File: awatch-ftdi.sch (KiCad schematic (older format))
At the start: 44 parts, among them J801 Molex 1050170001, J802 Conn_01x06, U801 AT93C46DN-SH-T, U802 MCP1703A-3302_SOT223, U803 FT2232HL, Y801 FH1200004

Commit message: approx. final layout
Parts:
- C801, C802, C803, C809, C810, C811, C812, C813, C814, C815, C816, C817, C818: value .1µF -> 0.1µF X7R; DigiKey PN (none) -> 1276-1061-1-ND
- C804, C806: value 4.7µF -> 4.7µF X7R; DigiKey PN (none) -> 1276-2087-1-ND
- C805, C807: value 22pF -> 22pF NP0; DigiKey PN (none) -> 399-7874-1-ND
- C808: value 3.3µF -> 4.7µF X7R; DigiKey PN (none) -> 1276-2087-1-ND
- J801: DigiKey PN (none) -> WM1399CT-ND
- U801: DigiKey PN (none) -> AT93C46DN-SH-TCT-ND AT93C46DN-SH-TCT-ND
- U802: DigiKey PN (none) -> MCP1703AT-3302E/DBCT-ND
- U803: DigiKey PN (none) -> 768-1024-1-ND
- Y801: DigiKey PN (none) -> FH1200004CT-ND
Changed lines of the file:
@@
 $Descr A4 11693 8268
 encoding utf-8
-Sheet 8 9
+Sheet 8 10
 Title "AWatch2"
 Date ""
@@
 F 2 "Package_QFP:LQFP-64_10x10mm_P0.5mm" H 5750 4450 50  0001 C CNN
 F 3 "http://www.ftdichip.com/Products/ICs/FT2232H.html" H 5750 4450 50  0001 C CNN
+F 4 "768-1024-1-ND" H 0   0   50  0001 C CNN "DigiKey PN"
 	1    5750 4450
 	1    0    0    -1
@@
 F 2 "Package_TO_SOT_SMD:SOT-223-3_TabPin2" H 3650 2750 50  0001 C CNN
 F 3 "http://ww1.microchip.com/downloads/en/DeviceDoc/20005122B.pdf" H 3650 2500 50  0001 C CNN
+F 4 "MCP1703AT-3302E/DBCT-ND" H 0   0   50  0001 C CNN "DigiKey PN"
 	1    3650 2550
 	1    0    0    -1
@@
 F 2 "Package_SO:SOIC-8_3.9x4.9mm_P1.27mm" H 2150 5350 50  0001 C CNN
 F 3 "http://ww1.microchip.com/downloads/en/DeviceDoc/20001749K.pdf" H 2150 5350 50  0001 C CNN
+F 4 "AT93C46DN-SH-TCT-NDAT93C46DN-SH-TCT-ND" H 0   0   50  0001 C CNN "DigiKey PN"
 	1    2150 5350
 	1    0    0    -1
@@
 P 1250 5300
 F 0 "C801" H 1342 5346 50  0000 L CNN
-F 1 ".1µF" H 1342 5255 50  0000 L CNN
+F 1 "0.1µF X7R" H 1342 5255 50  0000 L CNN
 F 2 "Capacitor_SMD:C_0603_1608Metric" H 1250 5300 50  0001 C CNN
 F 3 "~" H 1250 5300 50  0001 C CNN
+F 4 "1276-1061-1-ND" H 0   0   50  0001 C CNN "DigiKey PN"
 	1    1250 5300
 	1    0    0    -1
@@
 P 4050 2700
 F 0 "C803" H 4142 2746 50  0000 L CNN
-F 1 ".1µF" H 4142 2655 50  0000 L CNN
+F 1 "0.1µF X7R" H 4142 2655 50  0000 L CNN
 F 2 "Capacitor_SMD:C_0603_1608Metric" H 4050 2700 50  0001 C CNN
 F 3 "~" H 4050 2700 50  0001 C CNN
+F 4 "1276-1061-1-ND" H 0   0   50  0001 C CNN "DigiKey PN"
 	1    4050 2700
 	1    0    0    -1
@@
 P 3150 2700
 F 0 "C802" H 3242 2746 50  0000 L CNN
-F 1 ".1µF" H 3242 2655 50  0000 L CNN
+F 1 "0.1µF X7R" H 3242 2655 50  0000 L CNN
 F 2 "Capacitor_SMD:C_0603_1608Metric" H 3150 2700 50  0001 C CNN
 F 3 "~" H 3150 2700 50  0001 C CNN
+F 4 "1276-1061-1-ND" H 0   0   50  0001 C CNN "DigiKey PN"
 	1    3150 2700
 	1    0    0    -1
@@
 P 4450 2950
 F 0 "C808" H 4358 2996 50  0000 R CNN
-F 1 "3.3µF" H 4358 2905 50  0000 R CNN
+F 1 "4.7µF X7R" H 4358 2905 50  0000 R CNN
 F 2 "Capacitor_SMD:C_0603_1608Metric" H 4450 2950 50  0001 C CNN
 F 3 "~" H 4450 2950 50  0001 C CNN
+F 4 "1276-2087-1-ND" H 0   0   50  0001 C CNN "DigiKey PN"
 	1    4450 2950
 	1    0    0    -1
@@
 P 4550 1500
 F 0 "C809" H 4642 1546 50  0000 L CNN
-F 1 ".1µF" H 4642 1455 50  0000 L CNN
+F 1 "0.1µF X7R" H 4642 1455 50  0000 L CNN
 F 2 "Capacitor_SMD:C_0603_1608Metric" H 4550 1500 50  0001 C CNN
 F 3 "~" H 4550 1500 50  0001 C CNN
+F 4 "1276-1061-1-ND" H 0   0   50  0001 C CNN "DigiKey PN"
 	1    4550 1500
 	1    0    0    -1
@@
 P 4750 1500
 F 0 "C810" H 4842 1546 50  0000 L CNN
-F 1 ".1µF" H 4842 1455 50  0000 L CNN
+F 1 "0.1µF X7R" H 4842 1455 50  0000 L CNN
 F 2 "Capacitor_SMD:C_0603_1608Metric" H 4750 1500 50  0001 C CNN
 F 3 "~" H 4750 1500 50  0001 C CNN
+F 4 "1276-1061-1-ND" H 0   0   50  0001 C CNN "DigiKey PN"
 	1    4750 1500
 	1    0    0    -1
@@
 P 6000 1150
 F 0 "C811" H 6092 1196 50  0000 L CNN
-F 1 ".1µF" H 6092 1105 50  0000 L CNN
+F 1 "0.1µF X7R" H 6092 1105 50  0000 L CNN
 F 2 "Capacitor_SMD:C_0603_1608Metric" H 6000 1150 50  0001 C CNN
 F 3 "~" H 6000 1150 50  0001 C CNN
+F 4 "1276-1061-1-ND" H 0   0   50  0001 C CNN "DigiKey PN"
 	1    6000 1150
 	1    0    0    -1
@@
 P 6350 1150
 F 0 "C812" H 6442 1196 50  0000 L CNN
-F 1 ".1µF" H 6442 1105 50  0000 L CNN
+F 1 "0.1µF X7R" H 6442 1105 50  0000 L CNN
 F 2 "Capacitor_SMD:C_0603_1608Metric" H 6350 1150 50  0001 C CNN
 F 3 "~" H 6350 1150 50  0001 C CNN
+F 4 "1276-1061-1-ND" H 0   0   50  0001 C CNN "DigiKey PN"
 	1    6350 1150
 	1    0    0    -1
@@
 P 6700 1150
 F 0 "C813" H 6792 1196 50  0000 L CNN
-F 1 ".1µF" H 6792 1105 50  0000 L CNN
+F 1 "0.1µF X7R" H 6792 1105 50  0000 L CNN
 F 2 "Capacitor_SMD:C_0603_1608Metric" H 6700 1150 50  0001 C CNN
 F 3 "~" H 6700 1150 50  0001 C CNN
+F 4 "1276-1061-1-ND" H 0   0   50  0001 C CNN "DigiKey PN"
 	1    6700 1150
 	1    0    0    -1
@@
 P 7050 1150
 F 0 "C814" H 7142 1196 50  0000 L CNN
-F 1 ".1µF" H 7142 1105 50  0000 L CNN
+F 1 "0.1µF X7R" H 7142 1105 50  0000 L CNN
 F 2 "Capacitor_SMD:C_0603_1608Metric" H 7050 1150 50  0001 C CNN
 F 3 "~" H 7050 1150 50  0001 C CNN
+F 4 "1276-1061-1-ND" H 0   0   50  0001 C CNN "DigiKey PN"
 	1    7050 1150
 	1    0    0    -1
@@
 P 7400 1150
 F 0 "C815" H 7492 1196 50  0000 L CNN
-F 1 ".1µF" H 7492 1105 50  0000 L CNN
+F 1 "0.1µF X7R" H 7492 1105 50  0000 L CNN
 F 2 "Capacitor_SMD:C_0603_1608Metric" H 7400 1150 50  0001 C CNN
 F 3 "~" H 7400 1150 50  0001 C CNN
+F 4 "1276-1061-1-ND" H 0   0   50  0001 C CNN "DigiKey PN"
 	1    7400 1150
 	1    0    0    -1
@@
 P 7750 1150
 F 0 "C816" H 7842 1196 50  0000 L CNN
-F 1 ".1µF" H 7842 1105 50  0000 L CNN
+F 1 "0.1µF X7R" H 7842 1105 50  0000 L CNN
 F 2 "Capacitor_SMD:C_0603_1608Metric" H 7750 1150 50  0001 C CNN
 F 3 "~" H 7750 1150 50  0001 C CNN
+F 4 "1276-1061-1-ND" H 0   0   50  0001 C CNN "DigiKey PN"
 	1    7750 1150
 	1    0    0    -1
@@
 P 8100 1150
 F 0 "C817" H 8192 1196 50  0000 L CNN
-F 1 ".1µF" H 8192 1105 50  0000 L CNN
+F 1 "0.1µF X7R" H 8192 1105 50  0000 L CNN
 F 2 "Capacitor_SMD:C_0603_1608Metric" H 8100 1150 50  0001 C CNN
 F 3 "~" H 8100 1150 50  0001 C CNN
+F 4 "1276-1061-1-ND" H 0   0   50  0001 C CNN "DigiKey PN"
 	1    8100 1150
 	1    0    0    -1
@@
 F 2 "Crystal:Crystal_SMD_2520-4Pin_2.5x2.0mm" H 3600 5850 50  0001 C CNN
 F 3 "~" H 3600 5850 50  0001 C CNN
+F 4 "FH1200004CT-ND" H 0   0   50  0001 C CNN "DigiKey PN"
 	1    3600 5850
 	0    1    1    0
@@
 P 4150 6250
 F 0 "C805" H 4242 6296 50  0000 L CNN
-F 1 "22pF" H 4242 6205 50  0000 L CNN
+F 1 "22pF NP0" H 4242 6205 50  0000 L CNN
 F 2 "Capacitor_SMD:C_0603_1608Metric" H 4150 6250 50  0001 C CNN
 F 3 "~" H 4150 6250 50  0001 C CNN
+F 4 "399-7874-1-ND" H 0   0   50  0001 C CNN "DigiKey PN"
 	1    4150 6250
 	1    0    0    -1
@@
 P 4350 6250
 F 0 "C807" H 4442 6296 50  0000 L CNN
-F 1 "22pF" H 4442 6205 50  0000 L CNN
+F 1 "22pF NP0" H 4442 6205 50  0000 L CNN
 F 2 "Capacitor_SMD:C_0603_1608Metric" H 4350 6250 50  0001 C CNN
 F 3 "~" H 4350 6250 50  0001 C CNN
+F 4 "399-7874-1-ND" H 0   0   50  0001 C CNN "DigiKey PN"
 	1    4350 6250
 	1    0    0    -1
@@
 F 2 "Connector_USB:USB_Micro-B_Molex-105017-0001" H 2150 3500 50  0001 C CNN
 F 3 "~" H 2150 3500 50  0001 C CNN
+F 4 "WM1399CT-ND" H 0   0   50  0001 C CNN "DigiKey PN"
 	1    2000 3550
 	1    0    0    -1
@@
 P 4150 1500
 F 0 "C804" H 4242 1546 50  0000 L CNN
-F 1 "4.7µF" H 4242 1455 50  0000 L CNN
+F 1 "4.7µF X7R" H 4242 1455 50  0000 L CNN
 F 2 "Capacitor_SMD:C_0603_1608Metric" H 4150 1500 50  0001 C CNN
 F 3 "~" H 4150 1500 50  0001 C CNN
+F 4 "1276-2087-1-ND" H 0   0   50  0001 C CNN "DigiKey PN"
 	1    4150 1500
 	-1   0    0    -1
@@
 P 4350 1500
 F 0 "C806" H 4442 1546 50  0000 L CNN
-F 1 "4.7µF" H 4442 1455 50  0000 L CNN
+F 1 "4.7µF X7R" H 4442 1455 50  0000 L CNN
 F 2 "Capacitor_SMD:C_0603_1608Metric" H 4350 1500 50  0001 C CNN
 F 3 "~" H 4350 1500 50  0001 C CNN
+F 4 "1276-2087-1-ND" H 0   0   50  0001 C CNN "DigiKey PN"
 	1    4350 1500
 	1    0    0    -1
@@
 P 4300 2700
 F 0 "C818" H 4392 2746 50  0000 L CNN
-F 1 ".1µF" H 4392 2655 50  0000 L CNN
+F 1 "0.1µF X7R" H 4392 2655 50  0000 L CNN
 F 2 "Capacitor_SMD:C_0603_1608Metric" H 4300 2700 50  0001 C CNN
 F 3 "~" H 4300 2700 50  0001 C CNN
+F 4 "1276-1061-1-ND" H 0   0   50  0001 C CNN "DigiKey PN"
 	1    4300 2700
 	1    0    0    -1

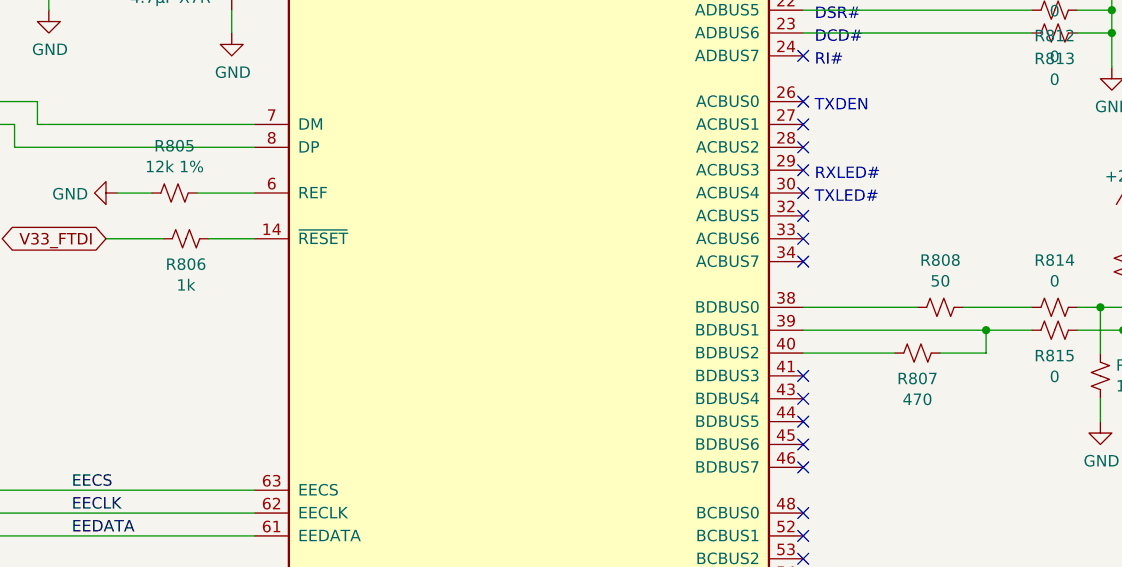
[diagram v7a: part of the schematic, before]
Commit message: BOM fully populated
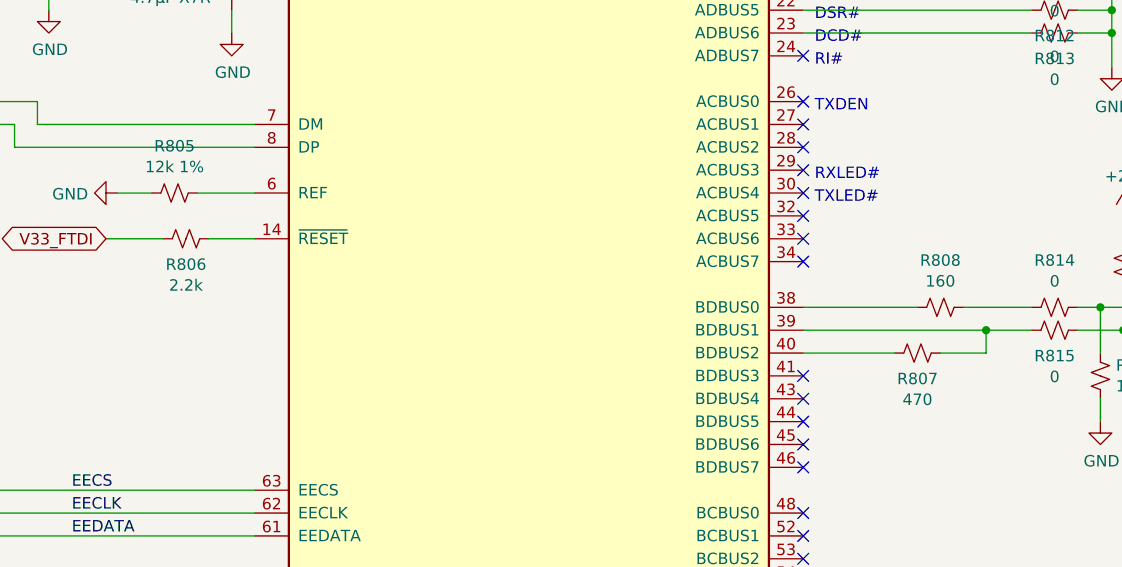
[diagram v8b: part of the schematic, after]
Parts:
- J802: DigiKey PN (none) -> S1011EC-06-ND
- L801, L802: DigiKey PN (none) -> 587-1926-1-ND
- R801, R803, R804, R816, R817: DigiKey PN (none) -> MCT0603-10.0K-CFCT-ND
- R802: DigiKey PN (none) -> MCT0603-2.20K-CFCT-ND
- R805: DigiKey PN (none) -> MCT0603-12.0K-CFCT-ND
- R806: value 1k -> 2.2k; DigiKey PN (none) -> MCT0603-2.20K-CFCT-ND
- R807: DigiKey PN (none) -> MCT0603-470-CFCT-ND
- R808: value 50 -> 160; DigiKey PN (none) -> 749-1765-1-ND
- R809, R810, R811, R812, R813, R814, R815: DigiKey PN (none) -> MCT0603-0.0-ZZCT-ND
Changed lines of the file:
@@
 P 7550 4350
 F 0 "R808" V 7345 4350 50  0000 C CNN
-F 1 "50" V 7436 4350 50  0000 C CNN
+F 1 "160" V 7436 4350 50  0000 C CNN
 F 2 "Resistor_SMD:R_0603_1608Metric" H 7550 4350 50  0001 C CNN
 F 3 "~" H 7550 4350 50  0001 C CNN
+F 4 "749-1765-1-ND" H 0   0   50  0001 C CNN "DigiKey PN"
 	1    7550 4350
 	0    1    1    0
@@
 F 2 "Resistor_SMD:R_0603_1608Metric" H 7450 4550 50  0001 C CNN
 F 3 "~" H 7450 4550 50  0001 C CNN
+F 4 "MCT0603-470-CFCT-ND" H 0   0   50  0001 C CNN "DigiKey PN"
 	1    7450 4550
 	0    1    1    0
@@
 F 2 "Resistor_SMD:R_0603_1608Metric" H 8050 4350 50  0001 C CNN
 F 3 "~" H 8050 4350 50  0001 C CNN
+F 4 "MCT0603-0.0-ZZCT-ND" H 0   0   50  0001 C CNN "DigiKey PN"
 	1    8050 4350
 	0    1    1    0
@@
 F 2 "Resistor_SMD:R_0603_1608Metric" H 8050 4450 50  0001 C CNN
 F 3 "~" H 8050 4450 50  0001 C CNN
+F 4 "MCT0603-0.0-ZZCT-ND" H 0   0   50  0001 C CNN "DigiKey PN"
 	1    8050 4450
 	0    1    1    0
@@
 F 2 "Resistor_SMD:R_0603_1608Metric" H 8250 4650 50  0001 C CNN
 F 3 "~" H 8250 4650 50  0001 C CNN
+F 4 "MCT0603-10.0K-CFCT-ND" H 0   0   50  0001 C CNN "DigiKey PN"
 	1    8250 4650
 	-1   0    0    1
@@
 F 2 "Resistor_SMD:R_0603_1608Metric" H 8350 4150 50  0001 C CNN
 F 3 "~" H 8350 4150 50  0001 C CNN
+F 4 "MCT0603-10.0K-CFCT-ND" H 0   0   50  0001 C CNN "DigiKey PN"
 	1    8350 4150
 	-1   0    0    1
@@
 F 2 "Resistor_SMD:R_0603_1608Metric" H 8050 2550 50  0001 C CNN
 F 3 "~" H 8050 2550 50  0001 C CNN
+F 4 "MCT0603-0.0-ZZCT-ND" H 0   0   50  0001 C CNN "DigiKey PN"
 	1    8050 2550
 	0    1    1    0
@@
 F 2 "Resistor_SMD:R_0603_1608Metric" H 8050 2650 50  0001 C CNN
 F 3 "~" H 8050 2650 50  0001 C CNN
+F 4 "MCT0603-0.0-ZZCT-ND" H 0   0   50  0001 C CNN "DigiKey PN"
 	1    8050 2650
 	0    1    1    0
@@
 F 2 "Resistor_SMD:R_0603_1608Metric" H 8050 2850 50  0001 C CNN
 F 3 "~" H 8050 2850 50  0001 C CNN
+F 4 "MCT0603-0.0-ZZCT-ND" H 0   0   50  0001 C CNN "DigiKey PN"
 	1    8050 2850
 	0    -1   -1   0
@@
 F 2 "Resistor_SMD:R_0603_1608Metric" H 8050 3050 50  0001 C CNN
 F 3 "~" H 8050 3050 50  0001 C CNN
+F 4 "MCT0603-0.0-ZZCT-ND" H 0   0   50  0001 C CNN "DigiKey PN"
 	1    8050 3050
 	0    -1   -1   0
@@
 F 2 "Resistor_SMD:R_0603_1608Metric" H 8050 3150 50  0001 C CNN
 F 3 "~" H 8050 3150 50  0001 C CNN
+F 4 "MCT0603-0.0-ZZCT-ND" H 0   0   50  0001 C CNN "DigiKey PN"
 	1    8050 3150
 	0    -1   -1   0
@@
 F 2 "Resistor_SMD:R_0603_1608Metric" H 2900 5450 50  0001 C CNN
 F 3 "~" H 2900 5450 50  0001 C CNN
+F 4 "MCT0603-2.20K-CFCT-ND" H 0   0   50  0001 C CNN "DigiKey PN"
 	1    2900 5450
 	0    1    1    0
@@
 F 2 "Resistor_SMD:R_0603_1608Metric" H 2800 4900 50  0001 C CNN
 F 3 "~" H 2800 4900 50  0001 C CNN
+F 4 "MCT0603-10.0K-CFCT-ND" H 0   0   50  0001 C CNN "DigiKey PN"
 	1    2800 4900
 	-1   0    0    1
@@
 F 2 "Resistor_SMD:R_0603_1608Metric" H 2950 4900 50  0001 C CNN
 F 3 "~" H 2950 4900 50  0001 C CNN
+F 4 "MCT0603-10.0K-CFCT-ND" H 0   0   50  0001 C CNN "DigiKey PN"
 	1    2950 4900
 	-1   0    0    1
@@
 F 2 "Resistor_SMD:R_0603_1608Metric" H 3100 4900 50  0001 C CNN
 F 3 "~" H 3100 4900 50  0001 C CNN
+F 4 "MCT0603-10.0K-CFCT-ND" H 0   0   50  0001 C CNN "DigiKey PN"
 	1    3100 4900
 	-1   0    0    1
@@
 F 2 "Resistor_SMD:R_0603_1608Metric" H 4200 3850 50  0001 C CNN
 F 3 "~" H 4200 3850 50  0001 C CNN
+F 4 "MCT0603-12.0K-CFCT-ND" H 0   0   50  0001 C CNN "DigiKey PN"
 	1    4200 3850
 	0    -1   -1   0
@@
 P 4250 4050
 F 0 "R806" V 4137 4050 50  0000 C CNN
-F 1 "1k" V 4046 4050 50  0000 C CNN
+F 1 "2.2k" V 4046 4050 50  0000 C CNN
 F 2 "Resistor_SMD:R_0603_1608Metric" H 4250 4050 50  0001 C CNN
 F 3 "~" H 4250 4050 50  0001 C CNN
+F 4 "MCT0603-2.20K-CFCT-ND" H 0   0   50  0001 C CNN "DigiKey PN"
 	1    4250 4050
 	0    -1   -1   0
@@
 F 2 "Inductor_SMD:L_0603_1608Metric" H 3850 1100 50  0001 C CNN
 F 3 "~" H 3850 1100 50  0001 C CNN
+F 4 "587-1926-1-ND" H 0   0   50  0001 C CNN "DigiKey PN"
 	1    3850 1100
 	0    -1   -1   0
@@
 F 2 "Inductor_SMD:L_0603_1608Metric" H 3850 1300 50  0001 C CNN
 F 3 "~" H 3850 1300 50  0001 C CNN
+F 4 "587-1926-1-ND" H 0   0   50  0001 C CNN "DigiKey PN"
 	1    3850 1300
 	0    -1   -1   0
@@
 F 2 "Connector_PinHeader_2.54mm:PinHeader_1x06_P2.54mm_Vertical" H 10200 2800 50  0001 C CNN
 F 3 "~" H 10200 2800 50  0001 C CNN
+F 4 "S1011EC-06-ND" H 0   0   50  0001 C CNN "DigiKey PN"
 	1    10200 2800
 	1    0    0    -1
